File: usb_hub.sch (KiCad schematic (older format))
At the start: 39 parts, among them U4 tusb2077a, Y3 Crystal_GND24

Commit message: cleaning up the usb hub schematic.
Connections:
- net labels added: D1_N, D1_P, D2_N, D2_P, D3_N, D3_P, D4_N, D4_P, DM1, DM2, DM3, DM4, DM5, DP1, DP2, DP3, DP4, DP5
- wire segments 81 -> 89
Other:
- moved on the sheet: C21, C22, C23, C24, C25, C26, C27, C28, C29, C30, R10, R11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

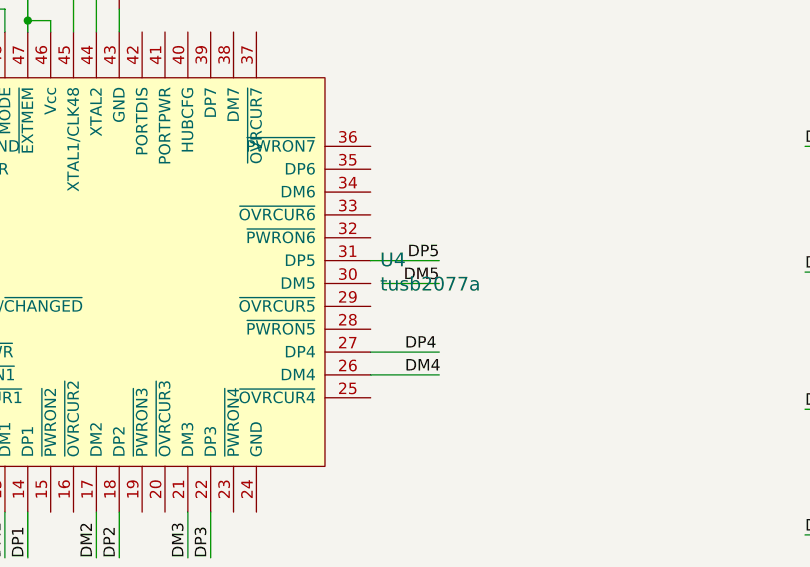
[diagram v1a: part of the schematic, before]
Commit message: schematics for expansion slots and memory
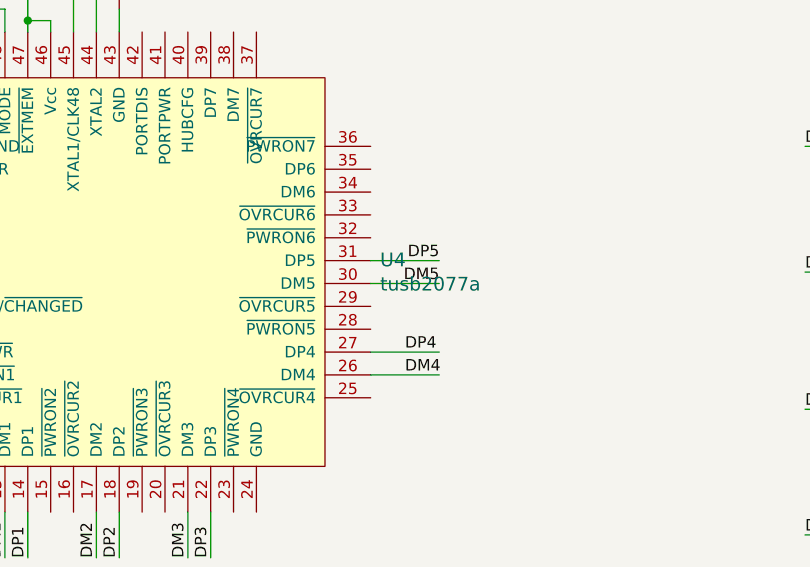
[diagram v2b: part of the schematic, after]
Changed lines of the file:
@@
 $Descr A4 11693 8268
 encoding utf-8
-Sheet 4 5
+Sheet 4 10
 Title ""
 Date ""
@@
 Wire Wire Line
 	6250 3650 6550 3650
-Wire Wire Line
-	6300 3750 6550 3750
 Text Label 6550 3650 2    50   ~ 0
 DP5
@@
 Text Label 8150 6000 0    50   ~ 0
 DM5
+Wire Wire Line
+	6250 3750 6550 3750
 $EndSCHEMATC

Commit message: almost done with draft 1 of layout
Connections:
- net DP0: now reaches R6.1, R8.2, U4.3 (DP0)
- net DM0: now reaches R7.1, U4.4 (DM0)
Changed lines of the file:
@@
 Wire Wire Line
 	6250 3750 6550 3750
+Text Label 3600 3350 0    50   ~ 0
+DP0
+Text Label 3600 3450 0    50   ~ 0
+DM0
 $EndSCHEMATC

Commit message: this is just a mess. but I think the schematic is basically right still.
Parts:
- removed C27, C28, C29, C30: C_Small, Capacitor_SMD:C_0603_1608Metric, symbol Device:C_Small
- removed R15, R16, R17, R18, R25, R26, R27, R28: R_Small, Resistor_SMD:R_0603_1608Metric, symbol Device:R_Small
- renumbered Y3 to Y1

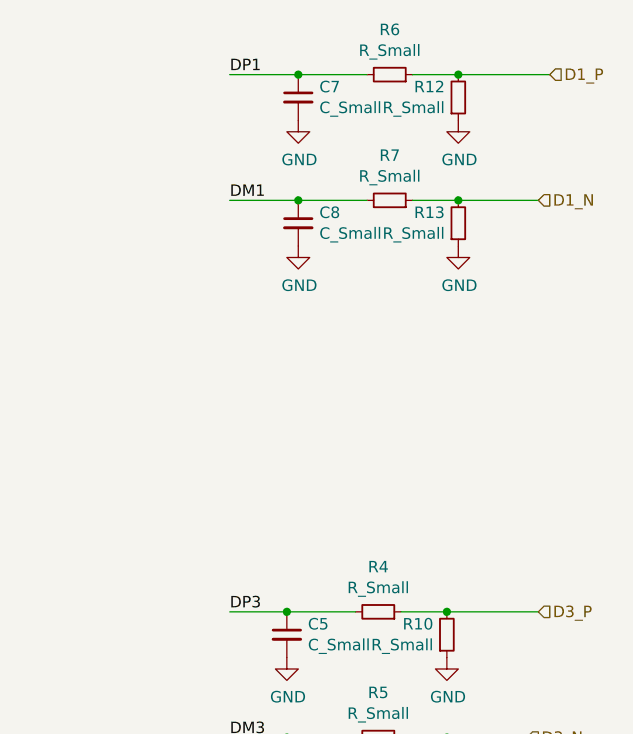
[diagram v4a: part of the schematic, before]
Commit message: picking this back up. Removing old unused schematic sheets.
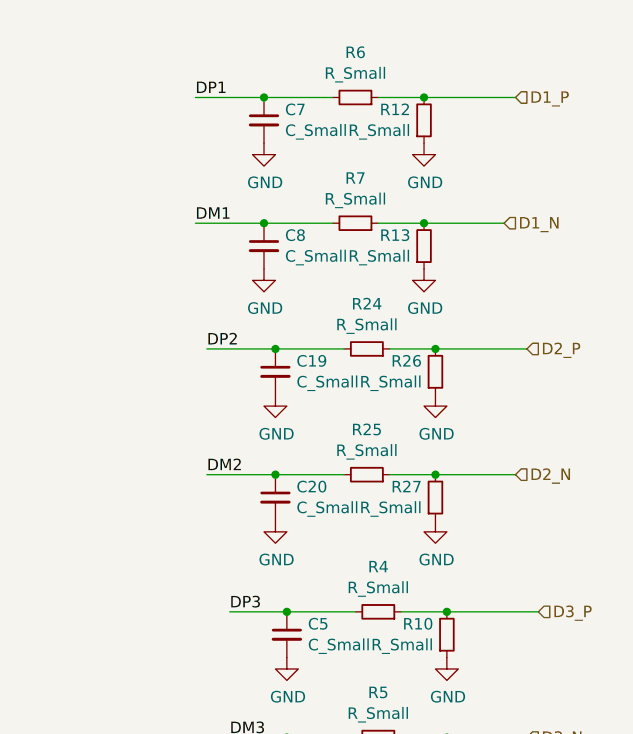
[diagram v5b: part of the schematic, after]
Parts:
- added C19, C20: C_Small, Capacitor_SMD:C_0603_1608Metric, symbol Device:C_Small
- added R24, R25, R26, R27: R_Small, Resistor_SMD:R_0603_1608Metric, symbol Device:R_Small
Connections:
- net DM2: now also C20.1, R25.2
- net DP2: now also C19.1, R24.2
- net GND: now also C19.2, C20.2, R26.1, R27.1
- new net D2_N: R25.1, R27.2
- new net D2_P: R24.1, R26.2
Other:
- moved on the sheet: C7, C8, R12, R13, R6, R7
